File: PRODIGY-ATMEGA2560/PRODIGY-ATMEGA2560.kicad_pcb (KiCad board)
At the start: 4 copper layers, 22 x 38 mm, 5 parts, among them J1 Bus_M.2_Socket_B, U1 ATmega2560-16A, U2 CH340G, Y1 Crystal

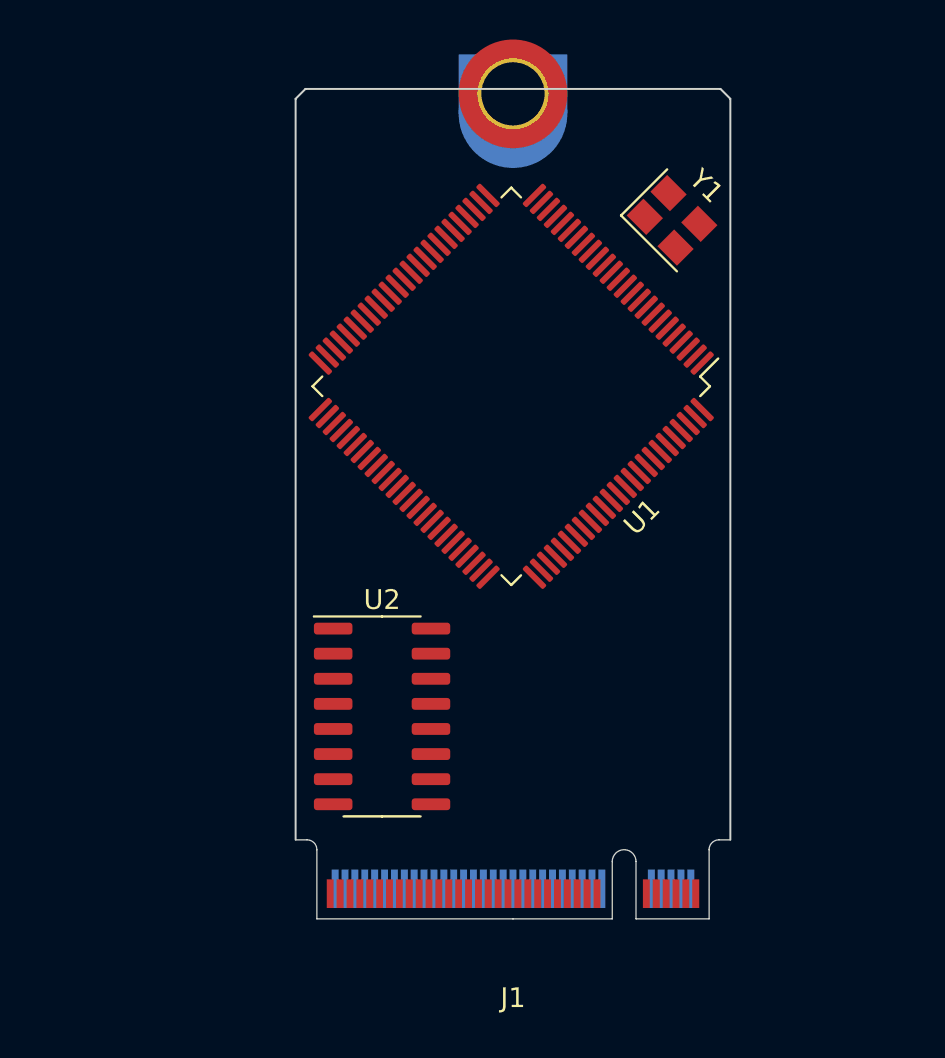
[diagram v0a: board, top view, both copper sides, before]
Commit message: ATMEGA2560 schematic finished
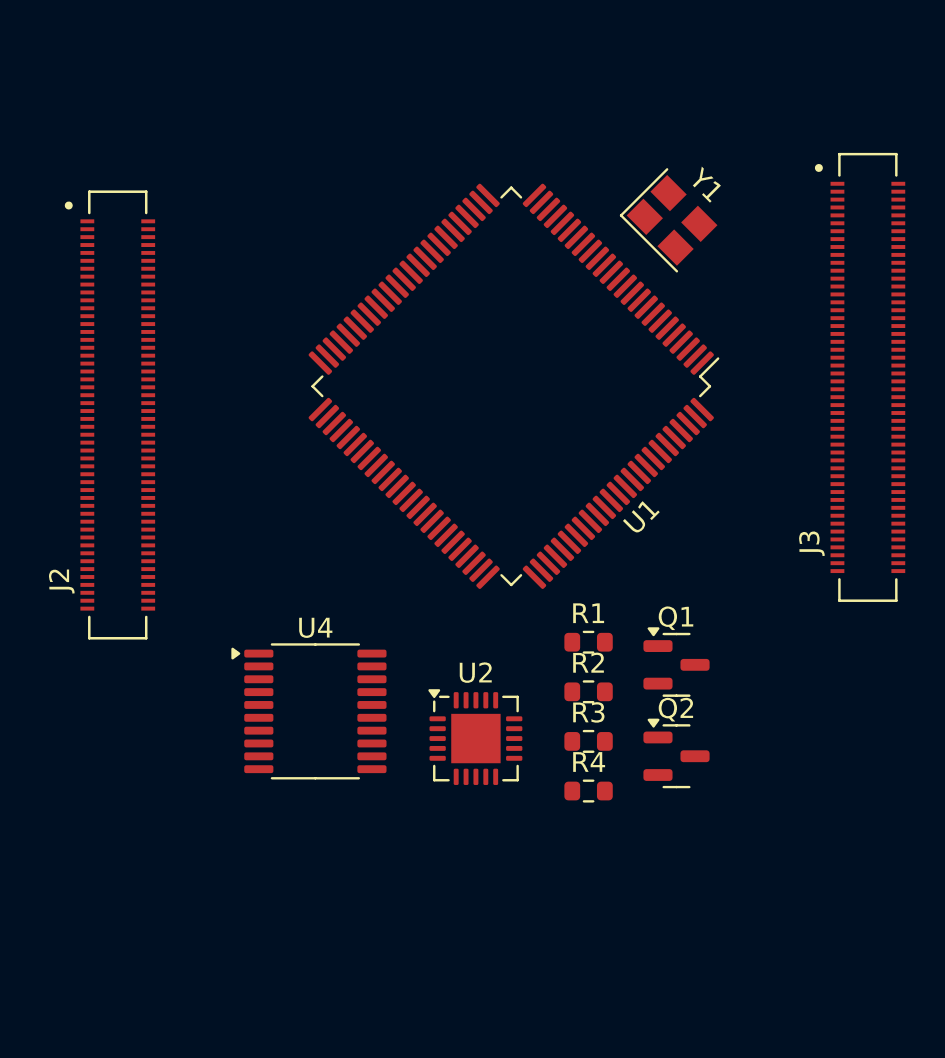
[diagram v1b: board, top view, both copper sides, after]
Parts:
- removed H1: MountingHole_Pad, Library:m.2_mounting_hole
- removed J1: Bus_M.2_Socket_B, NGFF:NGFF_B
- added J2: DF40C-100DS-0.4V(51), DF40C:HIROSE_DF40C-100DS-0.4V_51_, F.Cu at (97.0, 74.5)
- added J3: DF40C-100DS-0.4V(51), DF40C:HIROSE_DF40C-100DS-0.4V_51_, F.Cu at (135.0, 72.6)
- added Q1: BC850, Package_TO_SOT_SMD:SOT-23, F.Cu at (125.3, 87.1)
- added Q2: BC850, Package_TO_SOT_SMD:SOT-23, F.Cu at (125.3, 91.8)
- added R1: 0R, Resistor_SMD:R_0603_1608Metric, F.Cu at (120.8, 86.0)
- added R2: 0R, Resistor_SMD:R_0603_1608Metric, F.Cu at (120.8, 88.5)
- added R3: 10k, Resistor_SMD:R_0603_1608Metric, F.Cu at (120.8, 91.0)
- added R4: 10k, Resistor_SMD:R_0603_1608Metric, F.Cu at (120.8, 93.5)
- added U4: TXS0108EPW, Package_SO:TSSOP-20_4.4x6.5mm_P0.65mm, F.Cu at (107.0, 89.5)
- U2: value CH340G -> FT231XQ; footprint Package_SO:SOIC-16_3.9x9.9mm_P1.27mm -> Package_DFN_QFN:QFN-20-1EP_4x4mm_P0.5mm_EP2.5x2.5mm
- Y1: value Crystal -> 16MHz
- moved U2 4.88 mm to (115.1, 90.9)
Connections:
- U1 pad 1: unconnected-(U1-PG5-Pad1) -> /atmega2560/DIGITAL_LED_OUT_2
- U1 pad 10: Net-(U1-VCC-Pad10) -> +5V
- U1 pad 100: unconnected-(U1-AVCC-Pad100) -> +5V
- U1 pad 11: Net-(U1-GND-Pad11) -> GND
- U1 pad 12: unconnected-(U1-PH0-Pad12) -> /atmega2560/SERIAL_OUT_RX1
- U1 pad 13: unconnected-(U1-PH1-Pad13) -> /atmega2560/SERIAL_OUT_TX1
- U1 pad 15: unconnected-(U1-PH3-Pad15) -> /atmega2560/MOTOR_PWM_OUT_1
- U1 pad 16: unconnected-(U1-PH4-Pad16) -> /atmega2560/MOTOR_PWM_OUT_2
- U1 pad 17: unconnected-(U1-PH5-Pad17) -> /atmega2560/DIGITAL_LED_OUT_0
- U1 pad 18: unconnected-(U1-PH6-Pad18) -> /atmega2560/DIGITAL_LED_OUT_1
- U1 pad 19: unconnected-(U1-PB0-Pad19) -> /atmega2560/SPI_CS_BREAKOUT
- U1 pad 2: unconnected-(U1-PE0-Pad2) -> /atmega2560/DIGITAL_IR_RECEIVER
- U1 pad 20: unconnected-(U1-PB1-Pad20) -> /atmega2560/SD_SCK
- U1 pad 21: unconnected-(U1-PB2-Pad21) -> /atmega2560/SD_MOSI
- U1 pad 22: unconnected-(U1-PB3-Pad22) -> /atmega2560/SD_MISO
- U1 pad 23: unconnected-(U1-PB4-Pad23) -> /atmega2560/DIGITAL_NEOPIXEL_OUT
- U1 pad 24: unconnected-(U1-PB5-Pad24) -> /atmega2560/DIGITAL_RGB_R
- U1 pad 25: unconnected-(U1-PB6-Pad25) -> /atmega2560/DIGITAL_RGB_G
- U1 pad 26: unconnected-(U1-PB7-Pad26) -> /atmega2560/DIGITAL_RGB_B
- U1 pad 28: unconnected-(U1-PG3-Pad28) -> /atmega2560/MOTOR_CC_IN_1
- U1 pad 29: unconnected-(U1-PG4-Pad29) -> /atmega2560/MOTOR_CC_IN_2
- U1 pad 3: unconnected-(U1-PE1-Pad3) -> /atmega2560/DIGITAL_IR_EMITTER
- U1 pad 30: unconnected-(U1-~{RESET}-Pad30) -> /atmega2560/MCU_RESET
- U1 pad 31: Net-(U1-VCC-Pad10) -> +5V
- U1 pad 32: Net-(U1-GND-Pad11) -> GND
- U1 pad 33: unconnected-(U1-XTAL2-Pad33) -> Net-(U1-XTAL2)
- U1 pad 34: unconnected-(U1-XTAL1-Pad34) -> Net-(U1-XTAL1)
- U1 pad 35: unconnected-(U1-PL0-Pad35) -> /atmega2560/MCU_GPIO_2
- U1 pad 36: unconnected-(U1-PL1-Pad36) -> /atmega2560/MCU_GPIO_3
- U1 pad 37: unconnected-(U1-PL2-Pad37) -> /atmega2560/MCU_GPIO_4
- U1 pad 38: unconnected-(U1-PL3-Pad38) -> /atmega2560/MCU_GPIO_5
- U1 pad 39: unconnected-(U1-PL4-Pad39) -> /atmega2560/MCU_GPIO_6
- U1 pad 40: unconnected-(U1-PL5-Pad40) -> /atmega2560/MCU_GPIO_7
- U1 pad 41: unconnected-(U1-PL6-Pad41) -> /atmega2560/MCU_GPIO_8
- U1 pad 42: unconnected-(U1-PL7-Pad42) -> /atmega2560/MCU_GPIO_9
- U1 pad 43: unconnected-(U1-PD0-Pad43) -> /atmega2560/I2C_SCL
- U1 pad 44: unconnected-(U1-PD1-Pad44) -> /atmega2560/I2C_SDA
- U1 pad 45: unconnected-(U1-PD2-Pad45) -> /atmega2560/USB_RX
- U1 pad 46: unconnected-(U1-PD3-Pad46) -> /atmega2560/USB_TX
- U1 pad 47: unconnected-(U1-PD4-Pad47) -> /atmega2560/DIGITAL_BUTTON_IN_0
- U1 pad 48: unconnected-(U1-PD5-Pad48) -> /atmega2560/DIGITAL_BUTTON_IN_1
- U1 pad 49: unconnected-(U1-PD6-Pad49) -> /atmega2560/DIGITAL_BUTTON_IN_2
- U1 pad 5: unconnected-(U1-PE3-Pad5) -> /atmega2560/DIGITAL_BUZZER_OUT
- U1 pad 50: unconnected-(U1-PD7-Pad50) -> /atmega2560/DIGITAL_BUTTON_IN_3
- U1 pad 53: unconnected-(U1-PC0-Pad53) -> /atmega2560/SPI_CS_SEVENSEG
- U1 pad 54: unconnected-(U1-PC1-Pad54) -> /atmega2560/SPI_CS_TFT
- U1 pad 55: unconnected-(U1-PC2-Pad55) -> /atmega2560/SPI_TFT_DC
- U1 pad 56: unconnected-(U1-PC3-Pad56) -> /atmega2560/SPI_TFT_RESET
- U1 pad 57: unconnected-(U1-PC4-Pad57) -> /atmega2560/SPI_CS_NFC
- U1 pad 58: unconnected-(U1-PC5-Pad58) -> /atmega2560/SPI_RST_NFC
- U1 pad 59: unconnected-(U1-PC6-Pad59) -> /atmega2560/SD_CS
- U1 pad 6: unconnected-(U1-PE4-Pad6) -> /atmega2560/DIGITAL_HEATER_OUT
- U1 pad 60: unconnected-(U1-PC7-Pad60) -> /atmega2560/SD_EN
- U1 pad 61: Net-(U1-VCC-Pad10) -> +5V
- U1 pad 62: Net-(U1-GND-Pad11) -> GND
- U1 pad 63: unconnected-(U1-PJ0-Pad63) -> /atmega2560/SERIAL_OUT_RX2
- U1 pad 64: unconnected-(U1-PJ1-Pad64) -> /atmega2560/SERIAL_OUT_TX2
- U1 pad 65: unconnected-(U1-PJ2-Pad65) -> /atmega2560/SD_DET
- U1 pad 69: unconnected-(U1-PJ6-Pad69) -> /atmega2560/MCU_GPIO_19
- U1 pad 7: unconnected-(U1-PE5-Pad7) -> /atmega2560/I2C_INTERRUPT_ACCEL
- U1 pad 71: unconnected-(U1-PA7-Pad71) -> /atmega2560/MCU_GPIO_10
- U1 pad 72: unconnected-(U1-PA6-Pad72) -> /atmega2560/MCU_GPIO_11
- U1 pad 73: unconnected-(U1-PA5-Pad73) -> /atmega2560/MCU_GPIO_12
- U1 pad 74: unconnected-(U1-PA4-Pad74) -> /atmega2560/MCU_GPIO_13
- U1 pad 75: unconnected-(U1-PA3-Pad75) -> /atmega2560/MCU_GPIO_14
- U1 pad 76: unconnected-(U1-PA2-Pad76) -> /atmega2560/MCU_GPIO_15
- U1 pad 77: unconnected-(U1-PA1-Pad77) -> /atmega2560/MCU_GPIO_16
- U1 pad 78: unconnected-(U1-PA0-Pad78) -> /atmega2560/MCU_GPIO_17
- U1 pad 79: unconnected-(U1-PJ7-Pad79) -> /atmega2560/MCU_GPIO_18
- U1 pad 8: unconnected-(U1-PE6-Pad8) -> /atmega2560/I2C_INTERRUPT_KEYPAD
- U1 pad 80: Net-(U1-VCC-Pad10) -> +5V
- U1 pad 81: Net-(U1-GND-Pad11) -> GND
- U1 pad 82: unconnected-(U1-PK7-Pad82) -> /atmega2560/MCU_GPIO_20
- U1 pad 83: unconnected-(U1-PK6-Pad83) -> /atmega2560/MCU_GPIO_21
- U1 pad 84: unconnected-(U1-PK5-Pad84) -> /atmega2560/MCU_GPIO_22
- U1 pad 85: unconnected-(U1-PK4-Pad85) -> /atmega2560/MCU_GPIO_23
- U1 pad 86: unconnected-(U1-PK3-Pad86) -> /atmega2560/MCU_GPIO_24
- U1 pad 87: unconnected-(U1-PK2-Pad87) -> /atmega2560/MCU_GPIO_25
- U1 pad 88: unconnected-(U1-PK1-Pad88) -> /atmega2560/MCU_GPIO_26
- U1 pad 89: unconnected-(U1-PK0-Pad89) -> /atmega2560/MCU_GPIO_27
- U1 pad 9: unconnected-(U1-PE7-Pad9) -> /atmega2560/SPI_IRQ_NFC
- U1 pad 90: unconnected-(U1-PF7-Pad90) -> /atmega2560/ANALOG_BREAKOUT_PIEZO
- U1 pad 91: unconnected-(U1-PF6-Pad91) -> /atmega2560/ANALOG_BREAKOUT_PT100
- U1 pad 92: unconnected-(U1-PF5-Pad92) -> /atmega2560/ANALOG_MICROPHONE
- U1 pad 93: unconnected-(U1-PF4-Pad93) -> /atmega2560/ANALOG_JOYSTICK_Y
- U1 pad 94: unconnected-(U1-PF3-Pad94) -> /atmega2560/ANALOG_JOYSTICK_X
- U1 pad 95: unconnected-(U1-PF2-Pad95) -> /atmega2560/ANALOG_PHOTOTRANSISTOR
- U1 pad 96: unconnected-(U1-PF1-Pad96) -> /atmega2560/ANALOG_HEATER_TEMPERATURE
- U1 pad 97: unconnected-(U1-PF0-Pad97) -> /atmega2560/ANALOG_POTENTIOMETER
- U1 pad 98: unconnected-(U1-AREF-Pad98) -> /atmega2560/MCU_VREF
- U1 pad 99: Net-(U1-GND-Pad11) -> GND
- U2 pad 1: unconnected-(U2-GND-Pad1) -> Net-(U2-RXD)
- U2 pad 10: unconnected-(U2-~{DSR}-Pad10) -> +5V
- U2 pad 12: unconnected-(U2-~{DCD}-Pad12) -> +5V
- U2 pad 13: unconnected-(U2-~{DTR}-Pad13) -> GND
- U2 pad 3: unconnected-(U2-RXD-Pad3) -> GND
- U2 pad 8: unconnected-(U2-XO-Pad8) -> /usbBridge/USB_DP
- U2 pad 9: unconnected-(U2-~{CTS}-Pad9) -> /usbBridge/USB_DM
- Y1 pad 1: unconnected-(Y1-Pad1) -> Net-(U1-XTAL2)
- Y1 pad 2: unconnected-(Y1-Pad2) -> Net-(U1-XTAL1)
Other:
- board outline removed

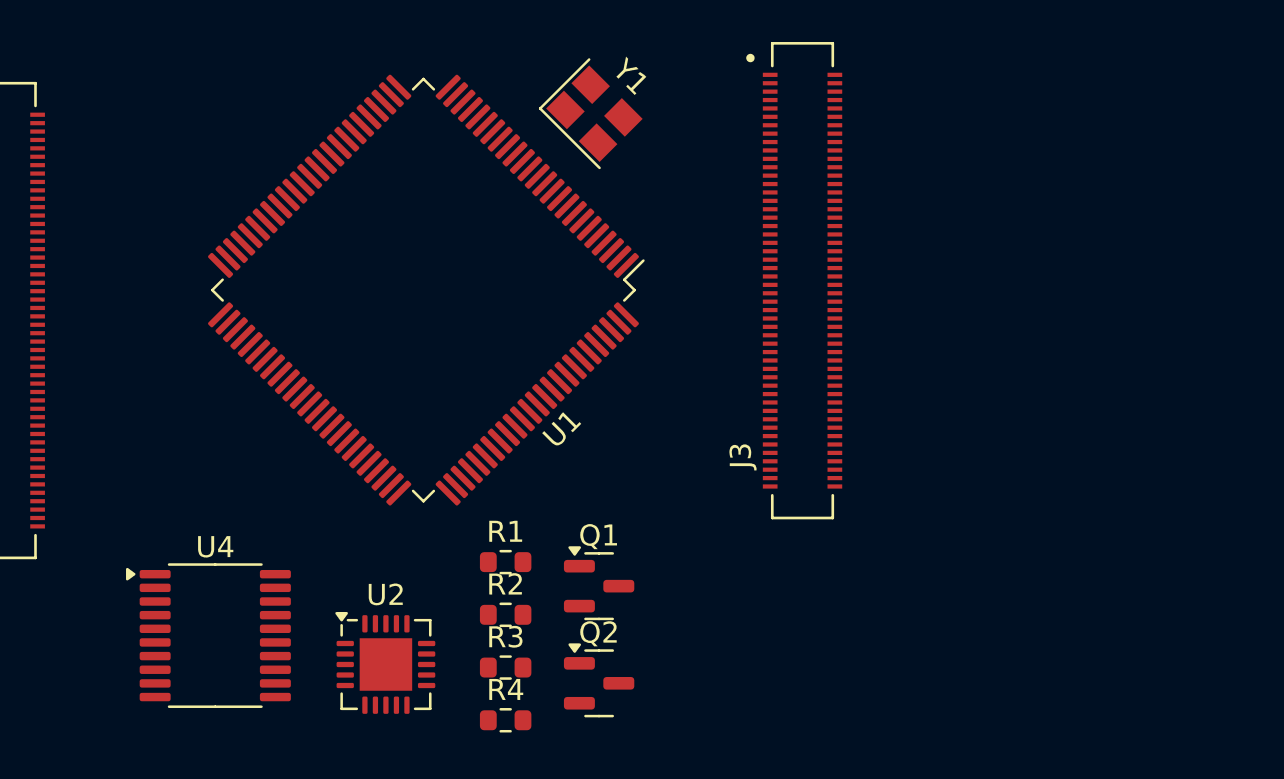
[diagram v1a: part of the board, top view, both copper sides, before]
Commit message: All footprint assosiations have been made across all schematics.
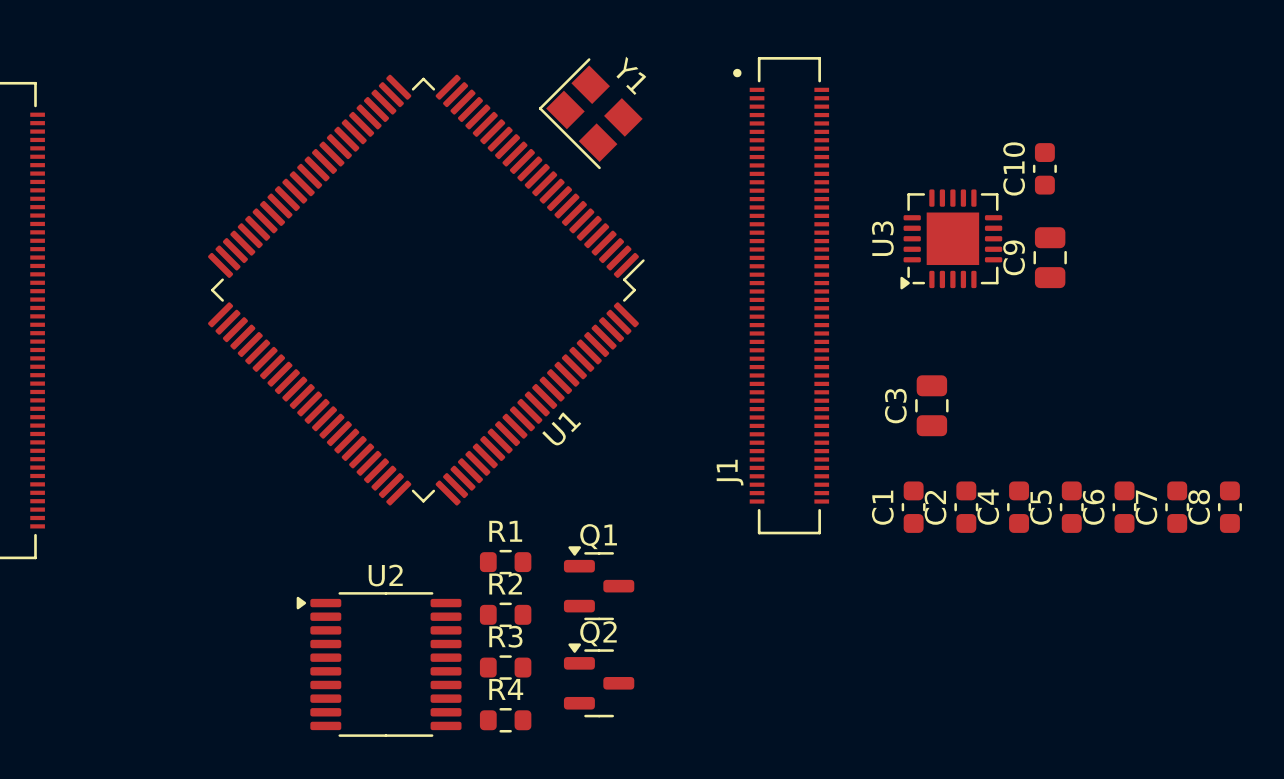
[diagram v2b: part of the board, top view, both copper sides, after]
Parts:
- removed J3: DF40C-100DS-0.4V(51), DF40C:HIROSE_DF40C-100DS-0.4V_51_
- removed U4: TXS0108EPW, Package_SO:TSSOP-20_4.4x6.5mm_P0.65mm
- added C1: 10pF, Capacitor_SMD:C_0603_1608Metric, F.Cu at (140.2, 83.4)
- added C10: 100nF, Capacitor_SMD:C_0603_1608Metric, F.Cu at (146.5, 67.3)
- added C2: 10pF, Capacitor_SMD:C_0603_1608Metric, F.Cu at (142.8, 83.4)
- added C3: 10uF, Capacitor_SMD:C_0805_2012Metric, F.Cu at (141.1, 78.6)
- added C4: 100nF, Capacitor_SMD:C_0603_1608Metric, F.Cu at (145.3, 83.4)
- added C5: 100nF, Capacitor_SMD:C_0603_1608Metric, F.Cu at (147.8, 83.4)
- added C6: 100nF, Capacitor_SMD:C_0603_1608Metric, F.Cu at (150.3, 83.4)
- added C7: 100nF, Capacitor_SMD:C_0603_1608Metric, F.Cu at (152.8, 83.4)
- added C8: 100nF, Capacitor_SMD:C_0603_1608Metric, F.Cu at (155.3, 83.4)
- added C9: 10uF, Capacitor_SMD:C_0805_2012Metric, F.Cu at (146.8, 71.5)
- added J1: DF40C-100DS-0.4V(51), DF40C:HIROSE_DF40C-100DS-0.4V_51_, F.Cu at (134.3, 73.3)
- added U3: FT231XQ, Package_DFN_QFN:QFN-20-1EP_4x4mm_P0.5mm_EP2.5x2.5mm, F.Cu at (142.1, 70.6)
- U2: value FT231XQ -> TXS0108EPW; footprint Package_DFN_QFN:QFN-20-1EP_4x4mm_P0.5mm_EP2.5x2.5mm -> Package_SO:TSSOP-20_4.4x6.5mm_P0.65mm
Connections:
- J2 pad 1: /connectorLeft/USB_HOST_FAULT -> GND
- J2 pad 10: /connectorLeft/SERIAL_OUT_TX2 -> unconnected-(J2-Pad10)
- J2 pad 100: /connectorLeft/ANALOG_BREAKOUT_PIEZO -> /atmega2560/MCU_RESET
- J2 pad 11: /connectorLeft/SERIAL_OUT_TX1 -> unconnected-(J2-Pad11)
- J2 pad 12: /connectorLeft/SERIAL_OUT_RX2 -> unconnected-(J2-Pad12)
- J2 pad 15: /connectorLeft/CAN_OUT_TX1 -> unconnected-(J2-Pad15)
- J2 pad 16: /connectorLeft/CAN_EN -> unconnected-(J2-Pad16)
- J2 pad 17: /connectorLeft/CAN_OUT_RX1 -> unconnected-(J2-Pad17)
- J2 pad 18: /connectorLeft/CAN_SILENT -> unconnected-(J2-Pad18)
- J2 pad 19: GND -> unconnected-(J2-Pad19)
- J2 pad 2: /connectorLeft/USB_HOST_ENABLE -> GND
- J2 pad 20: GND -> unconnected-(J2-Pad20)
- J2 pad 21: /connectorLeft/I2C_SDA -> unconnected-(J2-Pad21)
- J2 pad 22: /connectorLeft/SPI_MOSI -> GND
- J2 pad 23: /connectorLeft/I2C_SCL -> GND
- J2 pad 24: /connectorLeft/SPI_MISO -> /atmega2560/MCU_GPIO_26
- J2 pad 25: GND -> /atmega2560/MCU_GPIO_21
- J2 pad 26: GND -> /atmega2560/MCU_GPIO_19
- J2 pad 27: /connectorLeft/I2C_INTERRUPT_ACCEL -> /atmega2560/MCU_GPIO_20
- J2 pad 28: /connectorLeft/SPI_SCK -> /atmega2560/MCU_GPIO_13
- J2 pad 29: /connectorLeft/I2C_INTERRUPT_KEYPAD -> /atmega2560/MCU_GPIO_16
- J2 pad 3: /connectorLeft/USB_DM -> unconnected-(J2-Pad3)
- J2 pad 30: /connectorLeft/SPI_CS_BREAKOUT -> /atmega2560/MCU_GPIO_6
- J2 pad 31: GND -> /atmega2560/MCU_GPIO_12
- J2 pad 33: /connectorLeft/DIGITAL_IR_EMITTER -> GND
- J2 pad 34: /connectorLeft/SPI_CS_SEVENSEG -> /atmega2560/MCU_GPIO_5
- J2 pad 35: /connectorLeft/DIGITAL_IR_RECEIVER -> unconnected-(J2-Pad35)
- J2 pad 36: /connectorLeft/SPI_CS_TFT -> unconnected-(J2-Pad36)
- J2 pad 37: GND -> /atmega2560/MCU_GPIO_7
- J2 pad 38: GND -> /atmega2560/MCU_GPIO_11
- J2 pad 39: /connectorLeft/DIGITAL_NEOPIXEL_OUT -> /atmega2560/MCU_GPIO_8
- J2 pad 4: /connectorLeft/USB_HOST_OUT_P- -> unconnected-(J2-Pad4)
- J2 pad 40: /connectorLeft/SPI_TFT_DC -> /atmega2560/MCU_GPIO_9
- J2 pad 41: /connectorLeft/DIGITAL_RGB_R -> /atmega2560/MCU_GPIO_25
- J2 pad 42: /connectorLeft/SPI_TFT_RESET -> GND
- J2 pad 43: /connectorLeft/DIGITAL_RGB_G -> GND
- J2 pad 44: GND -> /atmega2560/MCU_GPIO_10
- J2 pad 45: /connectorLeft/DIGITAL_RGB_B -> /atmega2560/MCU_GPIO_24
- J2 pad 46: /connectorLeft/SPI_CS_NFC -> /atmega2560/MCU_GPIO_22
- J2 pad 47: /connectorLeft/DIGITAL_BUTTON_IN_0 -> /atmega2560/MCU_GPIO_23
- J2 pad 48: /connectorLeft/SPI_IRQ_NFC -> /atmega2560/MCU_GPIO_27
- J2 pad 49: /connectorLeft/DIGITAL_BUTTON_IN_1 -> /atmega2560/MCU_GPIO_18
- J2 pad 5: /connectorLeft/USB_DP -> unconnected-(J2-Pad5)
- J2 pad 50: GND -> /atmega2560/MCU_GPIO_17
- J2 pad 51: /connectorLeft/DIGITAL_BUTTON_IN_2 -> /atmega2560/MCU_GPIO_15
- J2 pad 52: /connectorLeft/SPI_RST_NFC -> GND
- J2 pad 53: /connectorLeft/DIGITAL_BUTTON_IN_3 -> GND
- J2 pad 54: /connectorLeft/DIGITAL_HEATER_OUT -> /atmega2560/MCU_GPIO_4
- J2 pad 55: GND -> /atmega2560/MCU_GPIO_14
- J2 pad 56: GND -> /atmega2560/MCU_GPIO_3
- J2 pad 57: /connectorLeft/DIGITAL_LED_OUT_0 -> /atmega2560/SD_CLK
- J2 pad 58: /connectorLeft/DIGITAL_LED_OUT_2 -> /atmega2560/MCU_GPIO_2
- J2 pad 59: /connectorLeft/DIGITAL_LED_OUT_1 -> GND
- J2 pad 6: /connectorLeft/USB_HOST_OUT_P+ -> unconnected-(J2-Pad6)
- J2 pad 60: /connectorLeft/DIGITAL_BUZZER_OUT -> GND
- J2 pad 61: GND -> /atmega2560/SD_DAT3
- J2 pad 62: GND -> /atmega2560/SD_CMD
- J2 pad 63: /connectorLeft/MOTOR_PWM_OUT_1 -> /atmega2560/SD_DAT1
- J2 pad 64: /connectorLeft/MOTOR_PWM_OUT_2 -> unconnected-(J2-Pad64)
- J2 pad 65: /connectorLeft/MOTOR_CC_IN_1 -> GND
- J2 pad 66: /connectorLeft/MOTOR_CC_IN_2 -> GND
- J2 pad 67: GND -> /atmega2560/SD_DAT0
- J2 pad 68: GND -> unconnected-(J2-Pad68)
- J2 pad 69: unconnected-(J2-Pad69) -> /atmega2560/SD_DAT2
- J2 pad 71: unconnected-(J2-Pad71) -> GND
- J2 pad 73: GND -> unconnected-(J2-Pad73)
- J2 pad 75: unconnected-(J2-Pad75) -> /atmega2560/SD_Enable
- J2 pad 76: unconnected-(J2-Pad76) -> /atmega2560/SD_DET
- J2 pad 77: unconnected-(J2-Pad77) -> +5V
- J2 pad 78: unconnected-(J2-Pad78) -> /connectorRight/MCU_VREF
- J2 pad 79: GND -> +5V
- J2 pad 80: GND -> unconnected-(J2-Pad80)
- J2 pad 81: /connectorLeft/ANALOG_PHOTOTRANSISTOR -> +5V
- J2 pad 82: /connectorLeft/ANALOG_POTENTIOMETER -> unconnected-(J2-Pad82)
- J2 pad 83: unconnected-(J2-Pad83) -> +5V
- J2 pad 84: unconnected-(J2-Pad84) -> +3V3
- J2 pad 85: GND -> +5V
- J2 pad 86: GND -> +3V3
- J2 pad 87: /connectorLeft/ANALOG_JOYSTICK_X -> +5V
- J2 pad 88: /connectorLeft/ANALOG_HEATER_TEMPERATURE -> +3V3
- J2 pad 9: /connectorLeft/SERIAL_OUT_RX1 -> unconnected-(J2-Pad9)
- J2 pad 90: unconnected-(J2-Pad90) -> +3V3
- J2 pad 91: GND -> unconnected-(J2-Pad91)
- J2 pad 92: GND -> unconnected-(J2-Pad92)
- J2 pad 93: /connectorLeft/ANALOG_JOYSTICK_Y -> unconnected-(J2-Pad93)
- J2 pad 94: /connectorLeft/ANALOG_BREAKOUT_PT100 -> unconnected-(J2-Pad94)
- J2 pad 97: GND -> unconnected-(J2-Pad97)
- J2 pad 99: /connectorLeft/ANALOG_MICROPHONE -> unconnected-(J2-Pad99)
- Q1 pad 3: /usbBridge/USB_RESET -> /atmega2560/MCU_RESET
- R1 pad 1: Net-(U2-TXD) -> Net-(U3-TXD)
- R1 pad 2: /usbBridge/USB_TX -> /atmega2560/USB_RX
- R2 pad 1: Net-(U2-RXD) -> Net-(U3-RXD)
- R2 pad 2: /usbBridge/USB_RX -> /atmega2560/USB_TX
- U1 pad 20: /atmega2560/SD_SCK -> /atmega2560/SCK
- U1 pad 21: /atmega2560/SD_MOSI -> /atmega2560/MOSI
- U1 pad 22: /atmega2560/SD_MISO -> /atmega2560/MISO
- U1 pad 98: /atmega2560/MCU_VREF -> unconnected-(U1-AREF-Pad98)
- U2 pad 1: Net-(U2-RXD) -> /atmega2560/SD_DET
- U2 pad 10: +5V -> +3.3V
- U2 pad 11: unconnected-(U2-~{RESET}-Pad11) -> GND
- U2 pad 12: +5V -> /atmega2560/SD_CS
- U2 pad 13: GND -> unconnected-(U2-B7-Pad13)
- U2 pad 15: unconnected-(U2-CBUS0-Pad15) -> /atmega2560/MISO
- U2 pad 16: unconnected-(U2-CBUS3-Pad16) -> /atmega2560/SCK
- U2 pad 17: Net-(U2-TXD) -> /atmega2560/MOSI
- U2 pad 18: /usbBridge/DTR -> /atmega2560/SD_EN
- U2 pad 19: /usbBridge/RTS -> +5V
- U2 pad 2: unconnected-(U2-~{RI}-Pad2) -> +3.3V
- U2 pad 20: +5V -> /atmega2560/SD_DET
- U2 pad 3: GND -> /atmega2560/SD_Enable
- U2 pad 4: unconnected-(U2-~{DSR}-Pad4) -> /atmega2560/SD_CMD
- U2 pad 5: unconnected-(U2-~{DCD}-Pad5) -> /atmega2560/SD_CLK
- U2 pad 6: unconnected-(U2-~{CTS}-Pad6) -> /atmega2560/SD_DAT0
- U2 pad 7: unconnected-(U2-CBUS2-Pad7) -> /atmega2560/SD_DAT1
- U2 pad 8: /usbBridge/USB_DP -> /atmega2560/SD_DAT2
- U2 pad 9: /usbBridge/USB_DM -> /atmega2560/SD_DAT3
